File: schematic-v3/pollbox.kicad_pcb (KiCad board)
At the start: 2 copper layers, 50.8 x 69.8 mm, 18 parts, among them P10 CONN_01X04, P2 CONN_02X03, P20 CONN_01X04, P30 CONN_01X04, P40 CONN_01X04, P50 CONN_01X04, U1 NodeMCU, U2 ULN2803

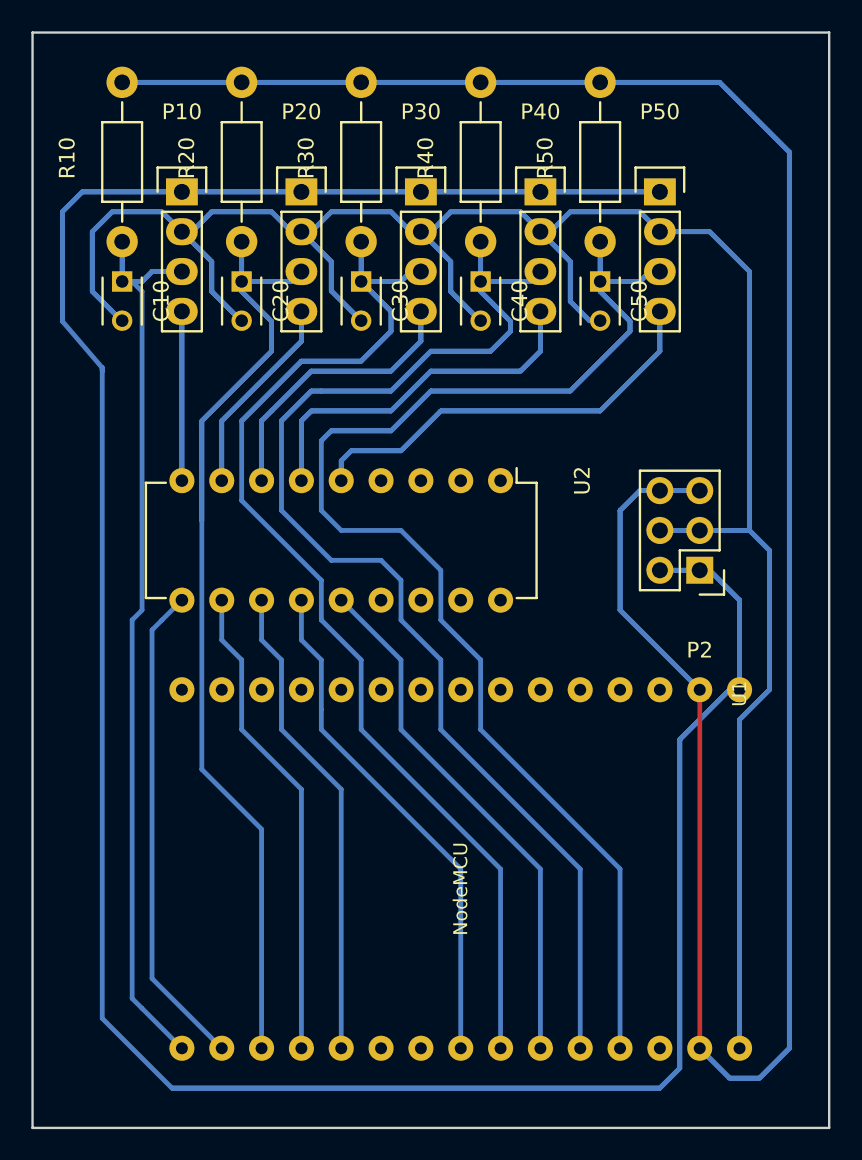
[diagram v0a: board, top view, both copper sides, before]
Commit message: feat: change track width on pcb
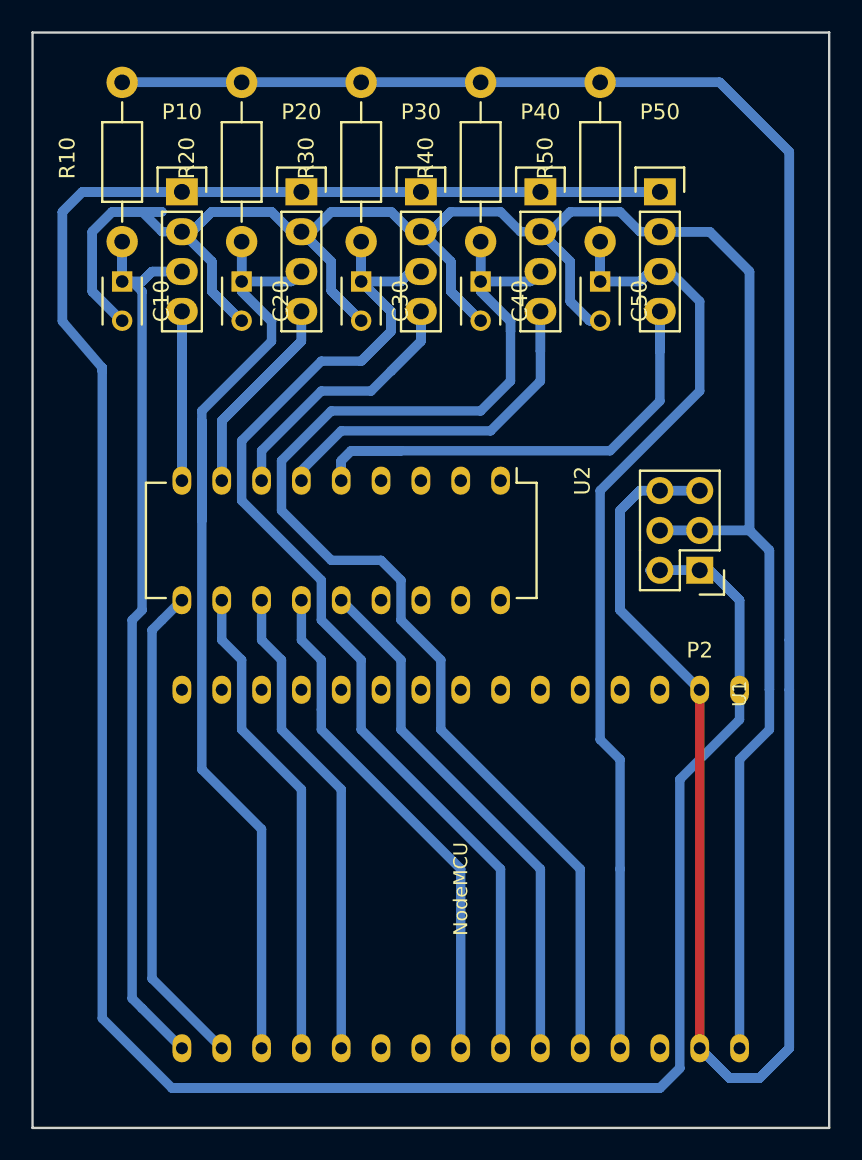
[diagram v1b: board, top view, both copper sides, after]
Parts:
- U1: footprint nodemcu:NodeMCU -> nodemcu:NodeMCU_oval_pads
- U2: footprint Housings_DIP:DIP-18_W7.62mm -> nodemcu:ULN2803_oval_pads
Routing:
- net /SWITCH_5: track 115.2 -> 67.3 mm
- net +3V3: track 280.2 -> 244.2 mm
- net +5V: track 285.7 -> 259.3 mm
- net /LED_4: track 46.9 -> 25.2 mm
- net /SWITCH_4: track 104.9 -> 88.3 mm
- net /LED_5: track 54.0 -> 39.3 mm
- net /LED_3: track 36.0 -> 21.5 mm
- net /SWITCH_3: track 91.8 -> 81.8 mm
- net /SWITCH_2: track 84.2 -> 76.0 mm
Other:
- net class Default: clearance 0.254 -> 0.3; trace_width 0.3048 -> 0.6
- rule trace_clearance: 0.254 -> 0.3
